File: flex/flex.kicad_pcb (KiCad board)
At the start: 2 copper layers, 74.1 x 41.5 mm, 30 parts, among them J1 Conn_01x06_Female, J2 Conn_01x03_Female, J3 Conn_01x01_Female, J4 Conn_01x01_Female, SW1 SW_Push, SW14 SW_Push, SW19 SW_Push, SW5 SW_Push, SW9 SW_Push

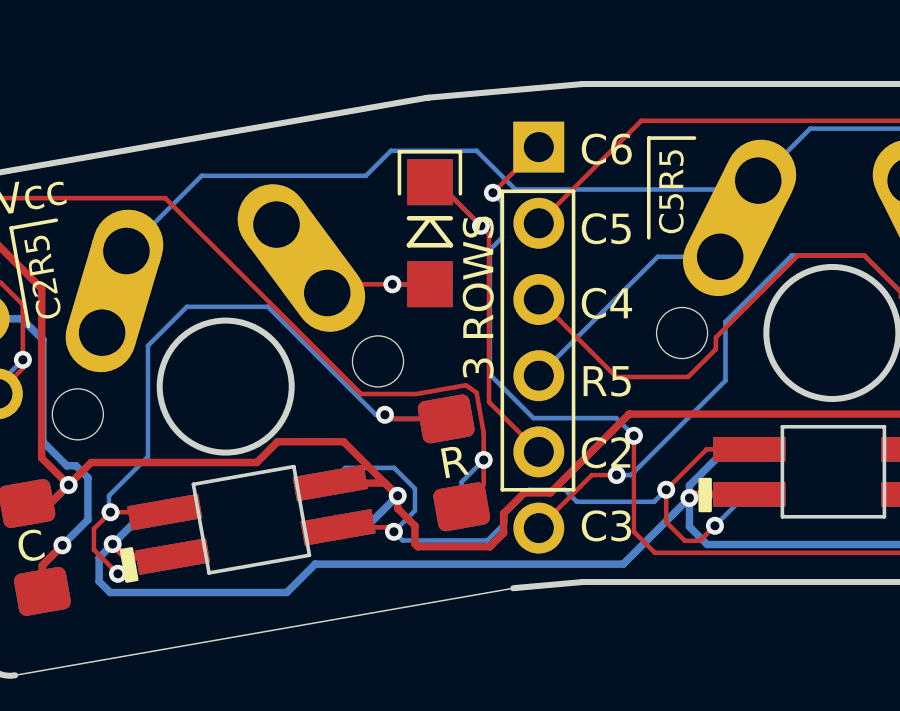
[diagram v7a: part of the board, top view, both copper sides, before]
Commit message: move r away from connector
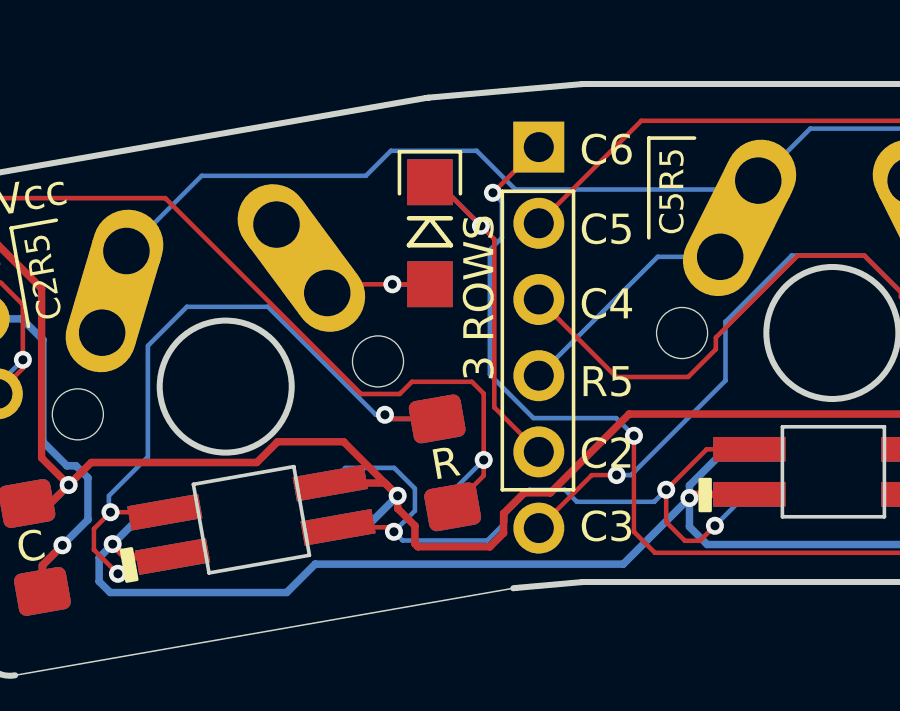
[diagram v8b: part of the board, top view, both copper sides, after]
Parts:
- moved R1 0.30 mm to (81.3, 78.9)
- moved R2 0.30 mm to (81.3, 78.9)
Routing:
- net Din: track 37.1 -> 37.8 mm
- net Net-(D12-Pad3): track 26.7 -> 26.1 mm
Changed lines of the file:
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@@
   )
   (footprint "Resistor_SMD:R_1206_3216Metric_Pad1.42x1.75mm_HandSolder" (layer "F.Cu")
-    (at 81.6 78.9 -80)
+    (at 81.3 78.9 -80)
     (descr "Resistor SMD 1206 (3216 Metric), square (rectangular) end terminal, IPC_7351 nominal with elongated pad for handsoldering. (Body size source: http://www.tortai-tech.com/upload/download/2011102023233369053.pdf), generated with kicad-footprint-generator")
     (tags "resistor handsolder")
@@
   )
   (footprint "Resistor_SMD:R_1206_3216Metric_Pad1.42x1.75mm_HandSolder" (layer "B.Cu")
-    (at 81.600868 78.904924 -80)
+    (at 81.3 78.904924 -80)
     (descr "Resistor SMD 1206 (3216 Metric), square (rectangular) end terminal, IPC_7351 nominal with elongated pad for handsoldering. (Body size source: http://www.tortai-tech.com/upload/download/2011102023233369053.pdf), generated with kicad-footprint-generator")
     (tags "resistor handsolder")
@@
     (effects (font (size 1.5 1.5) (thickness 0.2)) (justify mirror))
   )
-  (gr_text "R" (at 81.576089 78.971684 10) (layer "B.SilkS")
+  (gr_text "R" (at 81.3 79 10) (layer "B.SilkS")
     (effects (font (size 1 1) (thickness 0.15)) (justify mirror))
   )
@@
     (effects (font (size 0.8 0.8) (thickness 0.12)))
   )
-  (gr_text "R" (at 81.593911 78.9 10) (layer "F.SilkS")
+  (gr_text "R" (at 81.317822 78.928316 10) (layer "F.SilkS")
     (effects (font (size 1 1) (thickness 0.15)))
   )
@@
   (via (at 79.55 72.95) (size 0.6) (drill 0.3) (layers "F.Cu" "B.Cu") (net 3))
   (segment (start 81.05 72.95) (end 79.55 72.95) (width 0.1524) (layer "B.Cu") (net 3))
-  (segment (start 81.05 69.55) (end 82.768952 71.268952) (width 0.1524) (layer "F.Cu") (net 4))
-  (segment (start 82.768952 76.876152) (end 84.4296 78.5368) (width 0.1524) (layer "F.Cu") (net 4))
-  (segment (start 82.768952 71.268952) (end 82.768952 76.876152) (width 0.1524) (layer "F.Cu") (net 4))
+  (segment (start 82.944973 71.444973) (end 82.944973 77.052173) (width 0.1524) (layer "F.Cu") (net 4))
+  (segment (start 82.944973 77.052173) (end 84.4296 78.5368) (width 0.1524) (layer "F.Cu") (net 4))
+  (segment (start 81.05 69.55) (end 82.944973 71.444973) (width 0.1524) (layer "F.Cu") (net 4))
   (via (at 82.5 71) (size 0.6) (drill 0.3) (layers "F.Cu" "B.Cu") (net 4))
   (segment (start 81.05 69.55) (end 82.5 71) (width 0.1524) (layer "B.Cu") (net 4))
@@
   (segment (start 101.2 100.566953) (end 101.2 99.6) (width 0.25) (layer "B.Cu") (net 12))
   (segment (start 97.84 79.95) (end 99.339997 78.450003) (width 0.25) (layer "B.Cu") (net 12))
-  (segment (start 82.108059 76.391175) (end 82.35681 76.565352) (width 0.1524) (layer "F.Cu") (net 13))
-  (segment (start 82.35681 76.565352) (end 82.432437 76.994257) (width 0.1524) (layer "F.Cu") (net 13))
-  (segment (start 82.432437 76.994257) (end 82.593062 77.905203) (width 0.1524) (layer "F.Cu") (net 13))
-  (segment (start 67.232133 75.752823) (end 67.232133 75.467867) (width 0.1524) (layer "F.Cu") (net 13))
+  (segment (start 64.735898 72.9) (end 64.239592 72.403694) (width 0.1524) (layer "F.Cu") (net 13))
+  (segment (start 80.2 76.2) (end 82.2 76.2) (width 0.1524) (layer "F.Cu") (net 13))
+  (segment (start 67.232133 73.632133) (end 66.5 72.9) (width 0.1524) (layer "F.Cu") (net 13))
   (segment (start 67.232133 75.467867) (end 67.232133 73.632133) (width 0.1524) (layer "F.Cu") (net 13))
-  (segment (start 78.508235 76.608235) (end 80.340139 76.608235) (width 0.1524) (layer "F.Cu") (net 13))
   (segment (start 64.239592 70.796306) (end 64.958557 70.077341) (width 0.1524) (layer "F.Cu") (net 13))
-  (segment (start 82.593062 78.806938) (end 82.593062 79.630142) (width 0.1524) (layer "F.Cu") (net 13))
+  (segment (start 67.232133 75.752823) (end 67.232133 75.467867) (width 0.1524) (layer "F.Cu") (net 13))
   (segment (start 64.958557 70.077341) (end 71.977341 70.077341) (width 0.1524) (layer "F.Cu") (net 13))
-  (segment (start 67.232133 73.632133) (end 66.5 72.9) (width 0.1524) (layer "F.Cu") (net 13))
+  (segment (start 66.5 72.9) (end 64.735898 72.9) (width 0.1524) (layer "F.Cu") (net 13))
+  (segment (start 82.2 76.2) (end 82.593062 76.593062) (width 0.1524) (layer "F.Cu") (net 13))
+  (segment (start 82.593062 78.806938) (end 82.593062 79.330142) (width 0.1524) (layer "F.Cu") (net 13))
+  (segment (start 78.508235 76.608235) (end 79.791765 76.608235) (width 0.1524) (layer "F.Cu") (net 13))
   (segment (start 71.977341 70.077341) (end 78.508235 76.608235) (width 0.1524) (layer "F.Cu") (net 13))
-  (segment (start 64.735898 72.9) (end 64.239592 72.403694) (width 0.1524) (layer "F.Cu") (net 13))
+  (segment (start 82.593062 76.593062) (end 82.593062 78.806938) (width 0.1524) (layer "F.Cu") (net 13))
+  (segment (start 79.791765 76.608235) (end 80.2 76.2) (width 0.1524) (layer "F.Cu") (net 13))
+  (segment (start 82.593062 79.330142) (end 81.558302 80.364902) (width 0.1524) (layer "F.Cu") (net 13))
   (segment (start 66.382133 76.602823) (end 67.232133 75.752823) (width 0.1524) (layer "F.Cu") (net 13))
-  (segment (start 80.340139 76.608235) (end 82.000052 76.315547) (width 0.1524) (layer "F.Cu") (net 13))
-  (segment (start 82.593062 77.905203) (end 82.593062 78.806938) (width 0.1524) (layer "F.Cu") (net 13))
-  (segment (start 82.593062 79.630142) (end 81.858302 80.364902) (width 0.1524) (layer "F.Cu") (net 13))
-  (segment (start 82.000052 76.315547) (end 82.108059 76.391175) (width 0.1524) (layer "F.Cu") (net 13))
-  (segment (start 66.5 72.9) (end 64.735898 72.9) (width 0.1524) (layer "F.Cu") (net 13))
   (segment (start 64.239592 72.403694) (end 64.239592 70.796306) (width 0.1524) (layer "F.Cu") (net 13))
   (via (at 82.593062 78.806938) (size 0.6) (drill 0.3) (layers "F.Cu" "B.Cu") (net 13))
   (via (at 67.232133 75.467867) (size 0.6) (drill 0.3) (layers "F.Cu" "B.Cu") (net 13))
   (segment (start 66.382133 76.602823) (end 66.382133 76.317867) (width 0.1524) (layer "B.Cu") (net 13))
-  (segment (start 81.85917 79.54083) (end 82.593062 78.806938) (width 0.1524) (layer "B.Cu") (net 13))
-  (segment (start 81.85917 80.369826) (end 81.85917 79.54083) (width 0.1524) (layer "B.Cu") (net 13))
+  (segment (start 81.558302 80.369826) (end 81.558302 79.841698) (width 0.1524) (layer "B.Cu") (net 13))
+  (segment (start 81.558302 79.841698) (end 82.593062 78.806938) (width 0.1524) (layer "B.Cu") (net 13))
   (segment (start 66.382133 76.317867) (end 67.232133 75.467867) (width 0.1524) (layer "B.Cu") (net 13))
   (segment (start 91.45 79.95) (end 89.57379 79.95) (width 0.25) (layer "F.Cu") (net 14))
@@
   (segment (start 79.889377 81.489377) (end 82.710623 81.489377) (width 0.1524) (layer "B.Cu") (net 19))
   (segment (start 77.982675 79.06973) (end 79.608209 79.06973) (width 0.1524) (layer "B.Cu") (net 19))
+  (segment (start 79.3 77.3) (end 79.435098 77.435098) (width 0.1524) (layer "F.Cu") (net 20))
   (segment (start 70.152391 80.547609) (end 71.962302 80.547609) (width 0.1524) (layer "F.Cu") (net 20))
   (segment (start 69.6 81.1) (end 70.152391 80.547609) (width 0.1524) (layer "F.Cu") (net 20))
-  (segment (start 79.435098 77.435098) (end 81.341698 77.435098) (width 0.1524) (layer "F.Cu") (net 20))
-  (segment (start 79.3 77.3) (end 79.435098 77.435098) (width 0.1524) (layer "F.Cu") (net 20))
   (segment (start 69.6 81.8) (end 69.6 81.1) (width 0.1524) (layer "F.Cu") (net 20))
   (segment (start 70.4 82.6) (end 69.6 81.8) (width 0.1524) (layer "F.Cu") (net 20))
+  (segment (start 79.435098 77.435098) (end 81.041698 77.435098) (width 0.1524) (layer "F.Cu") (net 20))
   (via (at 79.3 77.3) (size 0.6) (drill 0.3) (layers "F.Cu" "B.Cu") (net 20))
   (via (at 70.152391 80.547609) (size 0.6) (drill 0.3) (layers "F.Cu" "B.Cu") (net 20))
@@
   (segment (start 72.222774 82.024821) (end 70.975179 82.024821) (width 0.1524) (layer "B.Cu") (net 20))
   (segment (start 70.1 80) (end 70.1 80.495218) (width 0.1524) (layer "B.Cu") (net 20))
-  (segment (start 81.342566 77.440022) (end 79.440022 77.440022) (width 0.1524) (layer "B.Cu") (net 20))
+  (segment (start 81.041698 77.440022) (end 79.440022 77.440022) (width 0.1524) (layer "B.Cu") (net 20))
   (segment (start 79.3 77.3) (end 79 77.3) (width 0.1524) (layer "B.Cu") (net 20))
   (segment (start 71.4 75) (end 71.4 78.7) (width 0.1524) (layer "B.Cu") (net 20))
   (segment (start 70.975179 82.024821) (end 70.4 82.6) (width 0.1524) (layer "B.Cu") (net 20))
   (segment (start 79 77.3) (end 75.4 73.7) (width 0.1524) (layer "B.Cu") (net 20))
-  (segment (start 79.440022 77.440022) (end 79.3 77.3) (width 0.1524) (layer "B.Cu") (net 20))
   (segment (start 71.4 78.7) (end 70.1 80) (width 0.1524) (layer "B.Cu") (net 20))
+  (segment (start 79.440022 77.440022) (end 79.3 77.3) (width 0.1524) (layer "B.Cu") (net 20))
   (segment (start 75.4 73.7) (end 72.7 73.7) (width 0.1524) (layer "B.Cu") (net 20))
   (segment (start 72.7 73.7) (end 71.4 75) (width 0.1524) (layer "B.Cu") (net 20))
